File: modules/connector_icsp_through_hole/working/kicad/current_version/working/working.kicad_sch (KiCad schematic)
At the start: 1 part, among them J1 hi12x3p

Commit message: a few module fixes
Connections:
- net miso: now also J1.1 (Pin_1)
- net reset: now also J1.5 (Pin_5)
- net sck: now also J1.3 (Pin_3)
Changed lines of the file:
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@@
+    (stroke (width 0) (type default))
+  )
+  (wire (pts (xy 137.16 92.71) (xy 139.7 92.71))
     (stroke (width 0) (type default))
   )
@@
     (stroke (width 0) (type default))
   )
+  (wire (pts (xy 137.16 90.17) (xy 139.7 90.17))
+    (stroke (width 0) (type default))
+  )
   (wire (pts (xy 152.4 90.17) (xy 154.94 90.17))
     (stroke (width 0) (type default))
   )
+  (wire (pts (xy 137.16 95.25) (xy 139.7 95.25))
+    (stroke (width 0) (type default))
+  )

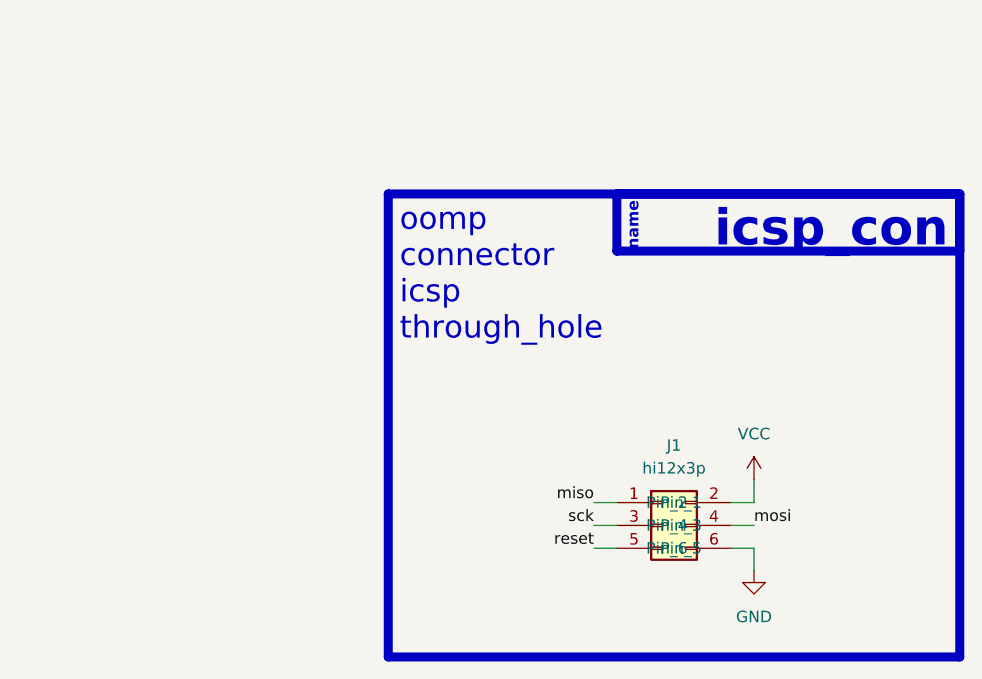
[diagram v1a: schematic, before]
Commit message: fixed formatting to be more consistent
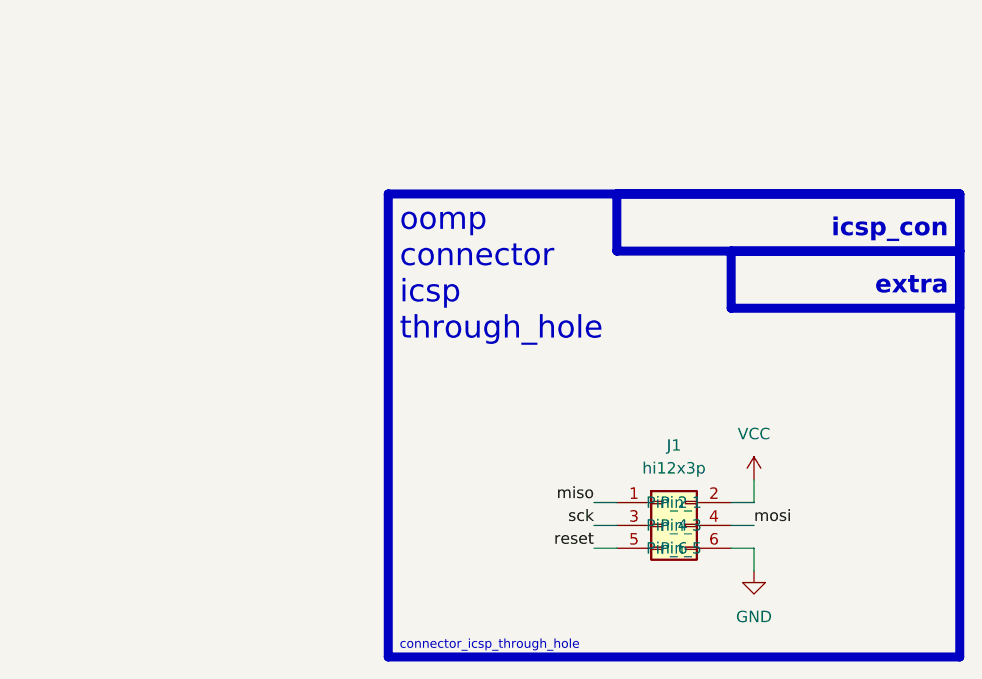
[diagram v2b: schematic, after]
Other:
- note added: "connector_icsp_through_hole"
- note added: "extra"
- note removed: "name"
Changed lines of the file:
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@@
   (rectangle (start 139.7 55.88) (end 177.8 62.23)
     (stroke (width 1) (type default))
-    (fill (type color) (color 0 0 0 0))
+    (fill (type none))
+  )
+  (rectangle (start 152.4 62.23) (end 177.8 68.58)
+    (stroke (width 1) (type default))
+    (fill (type none))
   )
   (rectangle (start 95.25 119.38) (end 95.25 119.38)
@@
     (effects (font (size 2.5 2.5)) (justify left bottom))
   )
-  (text "name" (at 142.24 62.23 90)
-    (effects (font (size 1.27 1.27) (thickness 0.254) bold (color 255 255 255 1)) (justify left bottom))
+  (text "extra" (at 176.53 67.31 0)
+    (effects (font (size 2 2) (thickness 0.8) bold) (justify right bottom))
   )
-  (text "icsp_con" (at 176.53 62.23 0)
-    (effects (font (size 4 4) (thickness 0.8) bold (color 255 255 255 1)) (justify right bottom))
+  (text "icsp_con" (at 176.53 60.96 0)
+    (effects (font (size 2 2) (thickness 0.8) bold) (justify right bottom))
+  )
+  (text "connector_icsp_through_hole" (at 115.57 106.68 0)
+    (effects (font (size 1 1)) (justify left bottom))
   )
   (label "miso" (at 137.16 90.17 180) (fields_autoplaced)

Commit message: schematic formatting
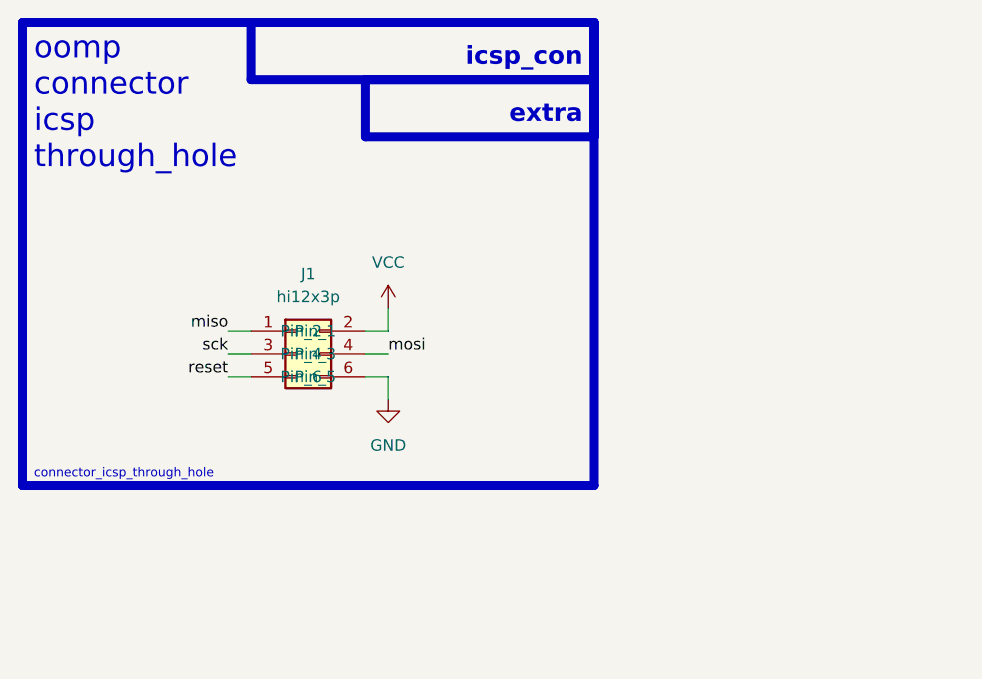
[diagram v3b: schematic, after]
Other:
- moved on the sheet: J1
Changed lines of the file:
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@@
 (kicad_sch (version 20230121) (generator eeschema)
-  (paper "A4")
-  (wire (pts (xy 152.4 95.25) (xy 154.94 95.25))
+  (paper "A5")
+  (wire (pts (xy 111.76 76.2) (xy 114.3 76.2))
     (stroke (width 0) (type default))
   )
-  (wire (pts (xy 137.16 92.71) (xy 139.7 92.71))
+  (wire (pts (xy 96.52 73.66) (xy 99.06 73.66))
     (stroke (width 0) (type default))
   )
-  (wire (pts (xy 154.94 95.25) (xy 154.94 97.79))
+  (wire (pts (xy 114.3 76.2) (xy 114.3 78.74))
     (stroke (width 0) (type default))
   )
-  (wire (pts (xy 154.94 90.17) (xy 154.94 87.63))
+  (wire (pts (xy 114.3 71.12) (xy 114.3 68.58))
     (stroke (width 0) (type default))
   )
-  (wire (pts (xy 152.4 92.71) (xy 154.94 92.71))
+  (wire (pts (xy 111.76 73.66) (xy 114.3 73.66))
     (stroke (width 0) (type default))
   )
-  (wire (pts (xy 137.16 90.17) (xy 139.7 90.17))
+  (wire (pts (xy 96.52 71.12) (xy 99.06 71.12))
     (stroke (width 0) (type default))
   )
-  (wire (pts (xy 152.4 90.17) (xy 154.94 90.17))
+  (wire (pts (xy 111.76 71.12) (xy 114.3 71.12))
     (stroke (width 0) (type default))
   )
-  (wire (pts (xy 137.16 95.25) (xy 139.7 95.25))
+  (wire (pts (xy 96.52 76.2) (xy 99.06 76.2))
     (stroke (width 0) (type default))
   )
-  (rectangle (start 139.7 55.88) (end 177.8 62.23)
+  (rectangle (start 99.06 36.83) (end 137.16 43.18)
     (stroke (width 1) (type default))
     (fill (type none))
   )
-  (rectangle (start 152.4 62.23) (end 177.8 68.58)
+  (rectangle (start 111.76 43.18) (end 137.16 49.53)
     (stroke (width 1) (type default))
     (fill (type none))
   )
-  (rectangle (start 95.25 119.38) (end 95.25 119.38)
+  (rectangle (start 54.61 100.33) (end 54.61 100.33)
     (stroke (width 0) (type default))
     (fill (type none))
   )
-  (rectangle (start 114.3 55.88) (end 177.8 107.3262)
+  (rectangle (start 73.66 36.83) (end 137.16 88.2762)
     (stroke (width 1) (type default))
     (fill (type none))
   )
-  (text "oomp\nconnector\nicsp\nthrough_hole\n" (at 115.57 72.39 0)
+  (text "oomp\nconnector\nicsp\nthrough_hole\n" (at 74.93 53.34 0)
     (effects (font (size 2.5 2.5)) (justify left bottom))
   )
-  (text "extra" (at 176.53 67.31 0)
+  (text "extra" (at 135.89 48.26 0)
     (effects (font (size 2 2) (thickness 0.8) bold) (justify right bottom))
   )
-  (text "icsp_con" (at 176.53 60.96 0)
+  (text "icsp_con" (at 135.89 41.91 0)
     (effects (font (size 2 2) (thickness 0.8) bold) (justify right bottom))
   )
-  (text "connector_icsp_through_hole" (at 115.57 106.68 0)
+  (text "connector_icsp_through_hole" (at 74.93 87.63 0)
     (effects (font (size 1 1)) (justify left bottom))
   )
-  (label "miso" (at 137.16 90.17 180) (fields_autoplaced)
+  (label "miso" (at 96.52 71.12 180) (fields_autoplaced)
     (effects (font (size 1.27 1.27)) (justify right bottom))
   )
-  (label "sck" (at 137.16 92.71 180) (fields_autoplaced)
+  (label "sck" (at 96.52 73.66 180) (fields_autoplaced)
     (effects (font (size 1.27 1.27)) (justify right bottom))
   )
-  (label "reset" (at 137.16 95.25 180) (fields_autoplaced)
+  (label "reset" (at 96.52 76.2 180) (fields_autoplaced)
     (effects (font (size 1.27 1.27)) (justify right bottom))
   )
-  (label "mosi" (at 154.94 92.71 0) (fields_autoplaced)
+  (label "mosi" (at 114.3 73.66 0) (fields_autoplaced)
     (effects (font (size 1.27 1.27)) (justify left bottom))
   )
-  (symbol (lib_id "power:GND") (at 154.94 97.79 0) (unit 1)
+  (symbol (lib_id "power:GND") (at 114.3 78.74 0) (unit 1)
     (in_bom yes) (on_board yes) (dnp no) (fields_autoplaced)
-    (property "Reference" "#PWR02" (at 154.94 104.14 0)
+    (property "Reference" "#PWR02" (at 114.3 85.09 0)
       (effects (font (size 1.27 1.27)) hide)
     )
-    (property "Value" "GND" (at 154.94 102.87 0)
+    (property "Value" "GND" (at 114.3 83.82 0)
       (effects (font (size 1.27 1.27)))
     )
-    (property "Footprint" "" (at 154.94 97.79 0)
+    (property "Footprint" "" (at 114.3 78.74 0)
       (effects (font (size 1.27 1.27)) hide)
     )
-    (property "Datasheet" "" (at 154.94 97.79 0)
+    (property "Datasheet" "" (at 114.3 78.74 0)
       (effects (font (size 1.27 1.27)) hide)
     )
@@
     )
   )
-  (symbol (lib_id "power:VCC") (at 154.94 87.63 0) (unit 1)
+  (symbol (lib_id "power:VCC") (at 114.3 68.58 0) (unit 1)
     (in_bom yes) (on_board yes) (dnp no) (fields_autoplaced)
-    (property "Reference" "#PWR01" (at 154.94 91.44 0)
+    (property "Reference" "#PWR01" (at 114.3 72.39 0)
       (effects (font (size 1.27 1.27)) hide)
     )
-    (property "Value" "VCC" (at 154.94 82.55 0)
+    (property "Value" "VCC" (at 114.3 63.5 0)
       (effects (font (size 1.27 1.27)))
     )
-    (property "Footprint" "" (at 154.94 87.63 0)
+    (property "Footprint" "" (at 114.3 68.58 0)
       (effects (font (size 1.27 1.27)) hide)
     )
-    (property "Datasheet" "" (at 154.94 87.63 0)
+    (property "Datasheet" "" (at 114.3 68.58 0)
       (effects (font (size 1.27 1.27)) hide)
     )
@@
     )
   )
-  (symbol (lib_id "oomlout_oomp_part_symbols:hi12x3p_electronic_header_2d54_mm_dual_row_2x3_dual_row_6_pin") (at 144.78 92.71 0) (unit 1)
+  (symbol (lib_id "oomlout_oomp_part_symbols:hi12x3p_electronic_header_2d54_mm_dual_row_2x3_dual_row_6_pin") (at 104.14 73.66 0) (unit 1)
     (in_bom yes) (on_board yes) (dnp no) (fields_autoplaced)
-    (property "Reference" "J1" (at 146.05 83.82 0)
+    (property "Reference" "J1" (at 105.41 64.77 0)
       (effects (font (size 1.27 1.27)))
     )
-    (property "Value" "hi12x3p" (at 146.05 86.36 0)
+    (property "Value" "hi12x3p" (at 105.41 67.31 0)
       (effects (font (size 1.27 1.27)))
     )
-    (property "Footprint" "hi12x3p_electronic_header_2d54_mm_dual_row_2x3_dual_row_6_pin" (at 144.78 92.71 0)
+    (property "Footprint" "hi12x3p_electronic_header_2d54_mm_dual_row_2x3_dual_row_6_pin" (at 104.14 73.66 0)
       (effects (font (size 1.27 1.27)) hide)
     )
-    (property "Datasheet" "https://github.com/oomlout/oomlout_oomp_v3/parts/electronic_header_2d54_mm_dual_row_2x3_dual_row_6_pin/datasheet.pdf" (at 144.78 92.71 0)
+    (property "Datasheet" "https://github.com/oomlout/oomlout_oomp_v3/parts/electronic_header_2d54_mm_dual_row_2x3_dual_row_6_pin/datasheet.pdf" (at 104.14 73.66 0)
       (effects (font (size 1.27 1.27)) hide)
     )
